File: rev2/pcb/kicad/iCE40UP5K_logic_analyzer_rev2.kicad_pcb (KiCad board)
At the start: 4 copper layers, 91.7 x 90.5 mm, 170 parts, among them IC1 ICE40UP5K-SG48I, IC2 MIC5504-3.3YM5-TR, IC3 MIC5504-1.2YM5-TR, IC4 FT2232HL-TRAY, IC5 W25Q40CLSNIG, IC6 SN74LVC14ADBRE4, IC7 SN74LVC14ADBRE4, IC8 SN74LVC14ADBRE4, J1 USB B Female Connector, J2 61300611121, J3 61202021621, J4 61300821121, J5 61300821121, J6 61300311121, J7 61300621121, Q1 2N7002H6327XTSA2, Y1 830208214809

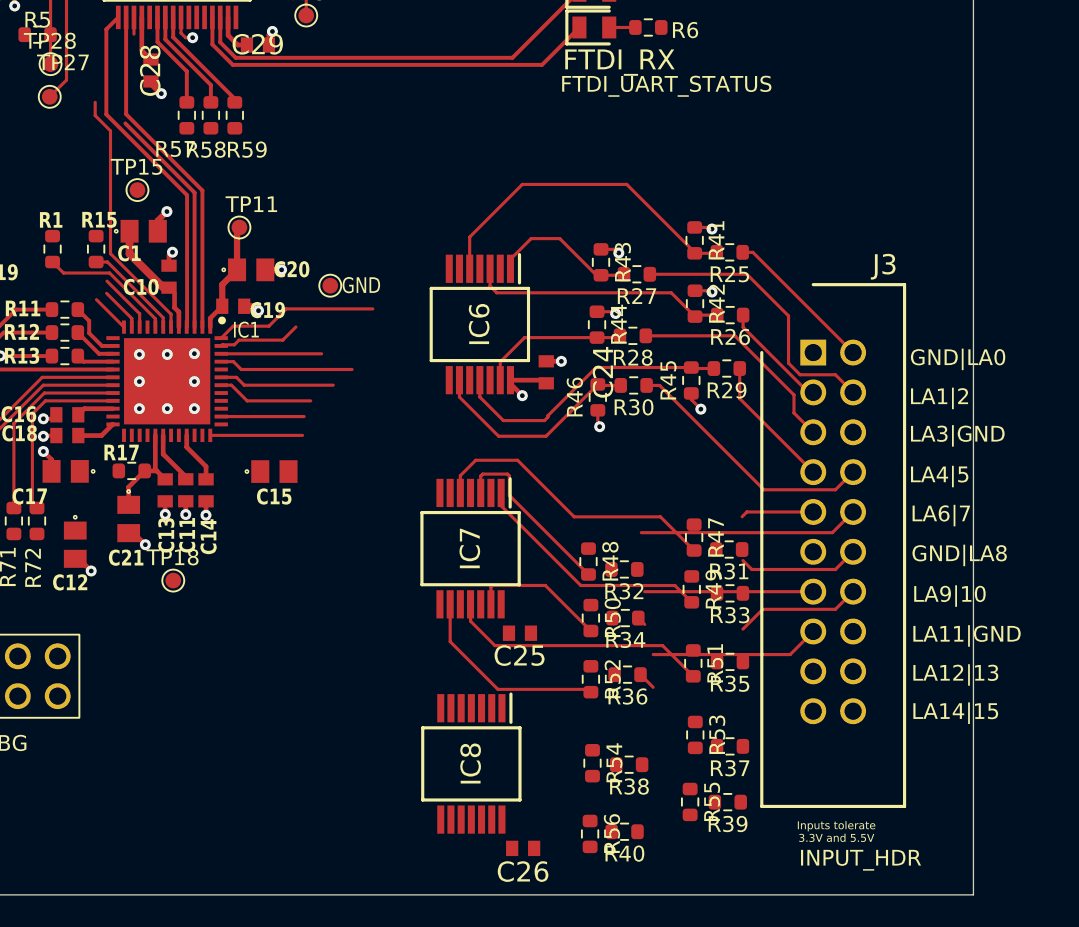
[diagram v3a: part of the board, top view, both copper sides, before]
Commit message: LAYOUT. LA inputs sorted. Note that LA12-15 have new FPGA pins (updated in notes table and PCF).
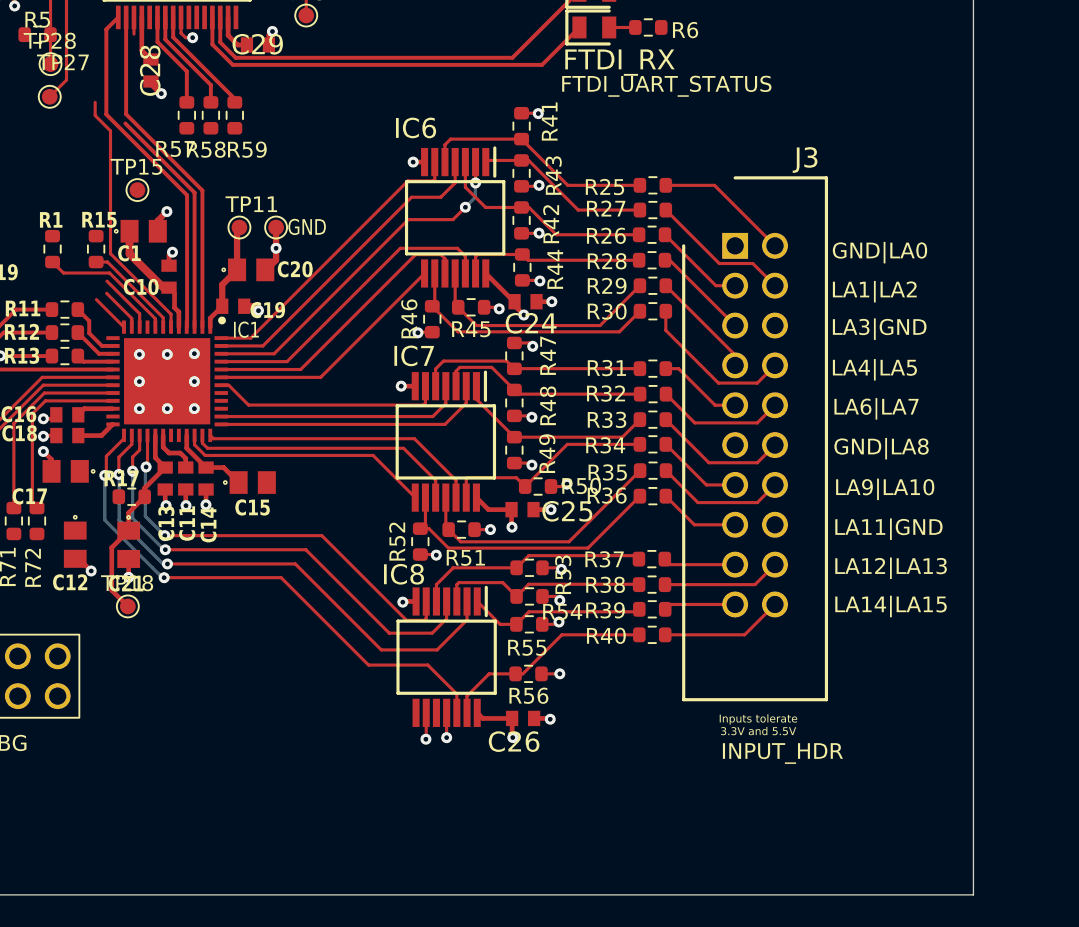
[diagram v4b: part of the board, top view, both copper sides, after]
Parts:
- moved R51 17.1 mm to (190.1, 129.1), turned to 180 degrees
- moved R47 16.3 mm to (193.5, 118.0)
- moved R55 15.3 mm to (194.5, 135.1), turned to 180 degrees
- moved R53 15.0 mm to (194.5, 131.5), turned to 180 degrees
- moved R45 14.8 mm to (190.7, 114.9), turned to 180 degrees
- moved R49 14.4 mm to (193.5, 124.0), turned to 90 degrees
- moved R52 14.0 mm to (187.5, 129.8), turned to 90 degrees
- moved R41 13.2 mm to (194.0, 103.4)
- moved R39 13.2 mm to (202.3, 134.2)
- moved R35 13.1 mm to (202.3, 125.3)
- moved R37 12.9 mm to (202.3, 131.0)
- moved R40 12.7 mm to (202.3, 135.8)
- moved R31 12.5 mm to (202.3, 118.8)
- moved R42 12.3 mm to (194.0, 109.4), turned to 90 degrees
- moved R33 12.1 mm to (202.3, 122.1)
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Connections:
- IC1 pad 25: unconnected-(IC1-IOT_36B-Pad25) -> /LA15
- IC1 pad 26: unconnected-(IC1-IOT_39A-Pad26) -> /LA14
- IC1 pad 27: /LA15 -> /LA13
- IC1 pad 28: /LA14 -> /LA12
- IC1 pad 31: /LA13 -> unconnected-(IC1-IOT_42B-Pad31)
- IC1 pad 32: /LA12 -> unconnected-(IC1-IOT_43A-Pad32)
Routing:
- net /LA15: track 0.00 -> 34.1 mm, vias 0 -> 2
- net /LA14: track 0.00 -> 33.3 mm, vias 0 -> 2
- net /LA13: track 0.00 -> 30.0 mm, vias 0 -> 2
- net /LA12: track 0.00 -> 27.0 mm, vias 0 -> 2
- net GND: track 132.0 -> 153.2 mm, vias 112 -> 129
- net /LA4: track 0.00 -> 18.3 mm
- net /LA10: track 0.00 -> 17.4 mm
- net /LA8: track 0.00 -> 17.3 mm
- net /LA2: track 11.8 -> 27.9 mm, vias 0 -> 2
- net /LA11: track 0.00 -> 16.1 mm
- net /LA1: track 9.01 -> 24.3 mm
- net Net-(IC8-3A): track 0.00 -> 14.8 mm
- net Net-(IC8-6A): track 0.00 -> 13.7 mm
- net Net-(IC8-2A): track 0.00 -> 13.4 mm
- net /LA9: track 13.2 -> 25.3 mm
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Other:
- board text added: "LA12|LA13"
- board text added: "LA14|LA15"
- board text added: "LA1|LA2"
- board text added: "LA4|LA5"
- board text added: "LA6|LA7"
- board text added: "LA9|LA10"
- board text removed: "LA12|13"
- board text removed: "LA14|15"
- board text removed: "LA1|2"
- board text removed: "LA4|5"
- board text removed: "LA6|7"
- board text removed: "LA9|10"

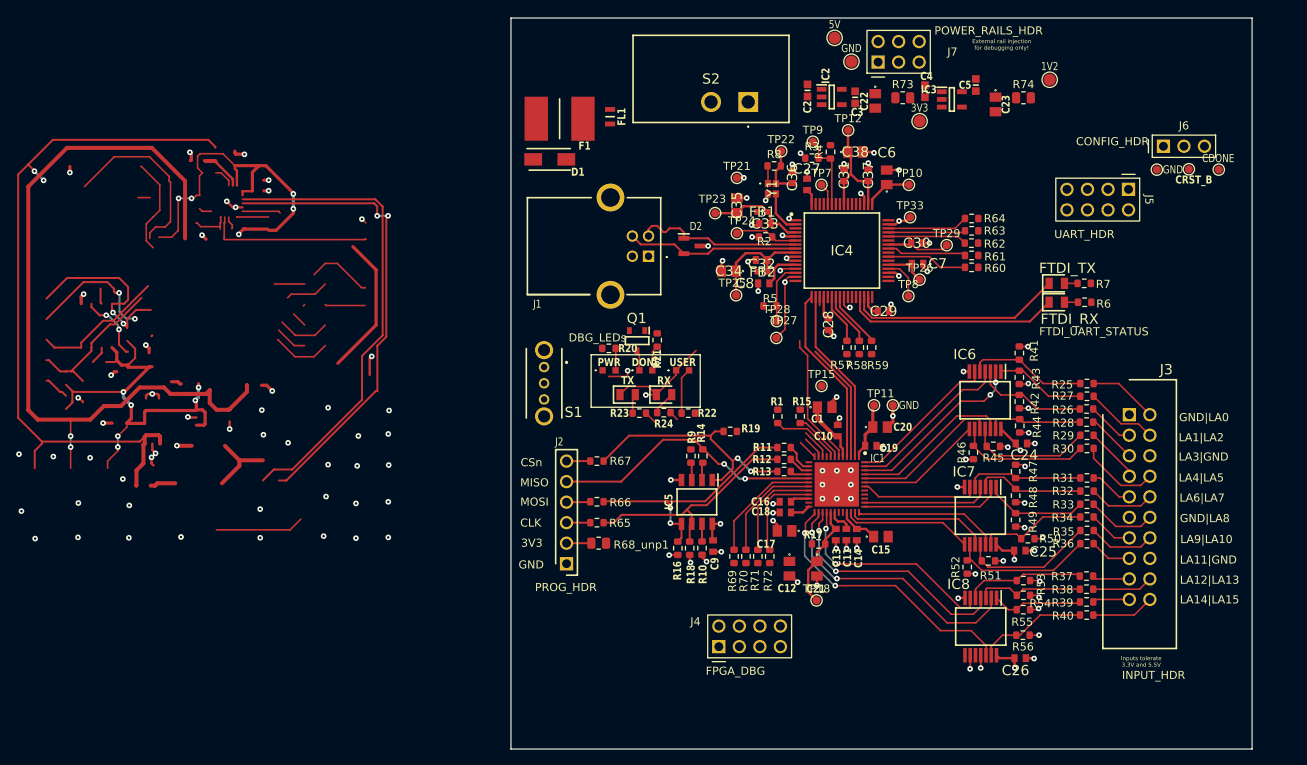
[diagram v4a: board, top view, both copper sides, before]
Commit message: LAYOUT. LEDs/DEBUG/HEADERS/testpads sorted.
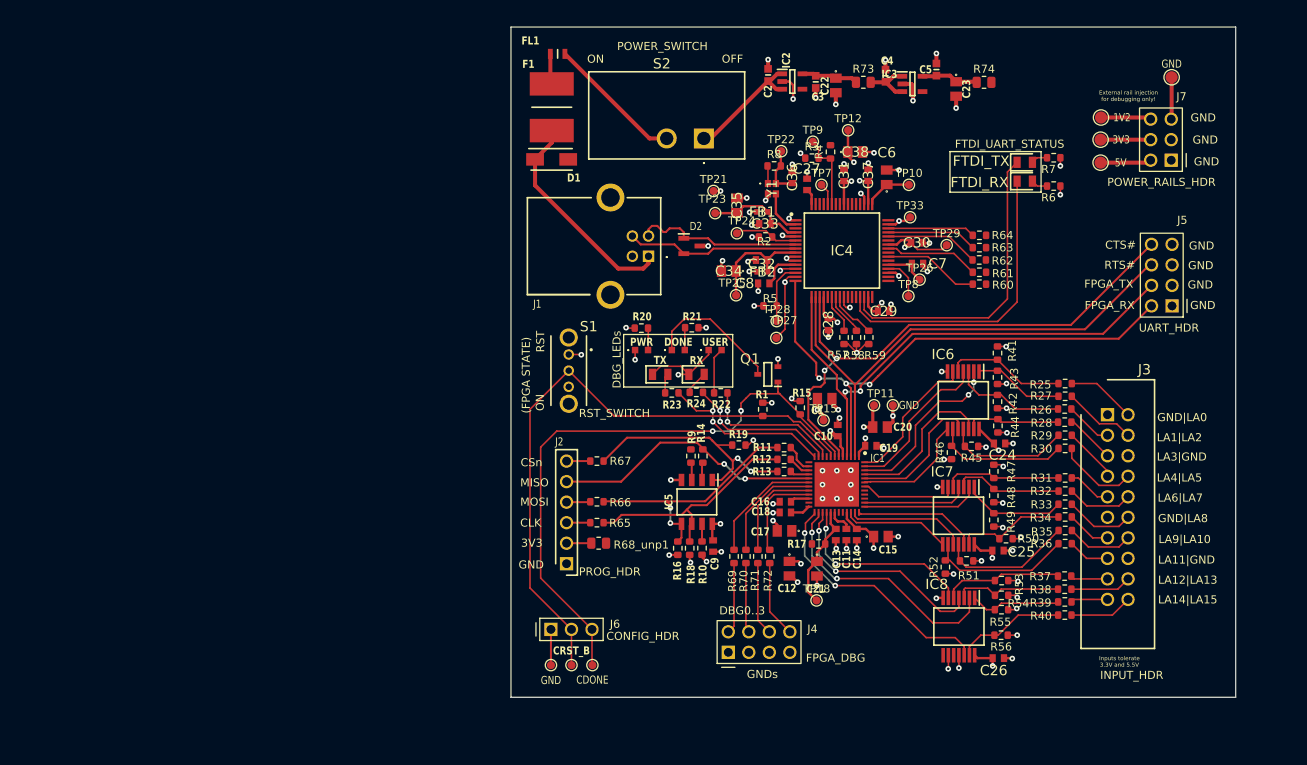
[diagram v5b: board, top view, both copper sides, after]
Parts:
- moved TP5 98.8 mm to (141.1, 142.0)
- moved TP6 98.0 mm to (138.5, 142.0)
- moved TP13 96.9 mm to (136.0, 142.0)
- moved J6 96.5 mm to (136.0, 137.6)
- moved TP4 39.7 mm to (212.8, 69.2)
- moved J7 38.2 mm to (212.8, 79.5), turned to 180 degrees
- moved TP1 36.4 mm to (204.0, 79.8)
- moved TP2 22.5 mm to (204.0, 77.0)
- moved Q1 16.7 mm to (162.8, 106.0), turned to 180 degrees
- moved R7 16.0 mm to (198.2, 79.2)
- moved D8 15.5 mm to (194.6, 82.1)
- moved D9 15.5 mm to (194.6, 79.8)
- moved J5 15.4 mm to (212.9, 97.5), turned to 180 degrees
- moved R6 14.9 mm to (198.2, 82.7)
- moved FL1 10.1 mm to (136.8, 66.3), turned to 180 degrees
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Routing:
- net +3V3: track 187.4 -> 91.9 mm, vias 17 -> 24
- net +1V2: track 107.1 -> 17.3 mm, vias 2 -> 3
- net +5V: track 89.9 -> 22.6 mm, vias 2 -> 1
- net /USB_D-: track 80.0 -> 21.0 mm
- net /USB_D+: track 79.7 -> 21.3 mm, vias 2 -> 0
- net /CRESET_B: track 20.6 -> 77.7 mm
- net /CTS#: track 17.4 -> 69.0 mm, vias 0 -> 2
- net /CDONE: track 28.8 -> 75.3 mm, vias 0 -> 2
- net /RTS#: track 21.8 -> 65.0 mm
- net /FPGA_UART_TX: track 27.0 -> 66.3 mm, vias 0 -> 2
- net /FPGA_UART_RX: track 35.1 -> 68.1 mm, vias 0 -> 3
- net /SPI_CSn: track 54.8 -> 30.8 mm, vias 4 -> 2
- net (no net): track 19.9 -> 0.00 mm
- net GND: track 153.2 -> 134.3 mm, vias 129 -> 90
- net /SPI_CLK: track 47.7 -> 29.1 mm
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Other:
- board size 91.7 x 90.5 mm -> 89.7 x 82.9 mm
- board text added: "(FPGA STATE)"
- board text added: "CTS#"
- board text added: "DBG0..3"
- board text added: "FPGA_RX"
- board text added: "FPGA_TX"
- board text added: "GNDs"
- board text added: "Logic Analyzer iCE40 UP5K Revision 2 26-06-2026 //JKO"
- board text added: "OFF"
- board text added: "ON"
- board text added: "POWER_SWITCH"
- board text added: "RST"
- board text added: "RST_SWITCH"
- board text added: "RTS#"
- board text removed: "Logic Analyzer iCE40 UP5K Revision 2 23-06-2026 //JKO"
